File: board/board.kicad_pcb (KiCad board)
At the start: 2 copper layers, 0 parts

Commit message: board: try different footprint placements
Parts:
- added REF**: USB_C_Receptacle_HRO_TYPE-C-31-M-17, Connector_USB:USB_C_Receptacle_HRO_TYPE-C-31-M-17, F.Cu at (163.4, 135.4)
- added REF**: USB_C_Receptacle_GCT_USB4105-xx-A_16P_TopMnt_Horizontal, Connector_USB:USB_C_Receptacle_GCT_USB4105-xx-A_16P_TopMnt_Horizontal, F.Cu at (70.9, 41.3)
- added REF**: PinHeader_2x15_P1.00mm_Vertical, Connector_PinHeader_1.00mm:PinHeader_2x15_P1.00mm_Vertical, F.Cu at (99.8, 123.7)
- added REF**: ProMicro_Reversible_Single, PCM_marbastlib-xp-promicroish:ProMicro_Reversible_Single, F.Cu at (84.0, 140.1)
- added REF**: Hirose_FH12-20S-0.5SH_1x20-1MP_P0.50mm_Horizontal, Connector_FFC-FPC:Hirose_FH12-20S-0.5SH_1x20-1MP_P0.50mm_Horizontal, F.Cu at (103.5, 107.0)
- added REF**: USB_C_Receptacle_HRO_TYPE-C-31-M-17, Connector_USB:USB_C_Receptacle_HRO_TYPE-C-31-M-17, F.Cu at (163.4, 123.6)
- added REF**: USB_C_Receptacle_GCT_USB4105-xx-A_16P_TopMnt_Horizontal, Connector_USB:USB_C_Receptacle_GCT_USB4105-xx-A_16P_TopMnt_Horizontal, F.Cu at (123.3, 101.9)
- added REF**: DF40C-40DS-0.4V, phiboard:DF40C-40DS-0.4V, F.Cu at (52.1, 35.6)
- added REF**: Raytac_MDBT50Q, RF_Module:Raytac_MDBT50Q, F.Cu at (59.8, 36.8)
- added REF**: PinHeader_2x11_P2.54mm_Vertical, Connector_PinHeader_2.54mm:PinHeader_2x11_P2.54mm_Vertical, F.Cu at (113.5, 149.1)
- added REF**: USB_C_Receptacle_GCT_USB4105-xx-A_16P_TopMnt_Horizontal, Connector_USB:USB_C_Receptacle_GCT_USB4105-xx-A_16P_TopMnt_Horizontal, F.Cu at (178.2, 121.3)
- added REF**: JST_EH_S2B-EH_1x02_P2.50mm_Horizontal, Connector_JST:JST_EH_S2B-EH_1x02_P2.50mm_Horizontal, F.Cu at (185.1, 137.2)
- added REF**: USB_C_Receptacle_GCT_USB4105-xx-A_16P_TopMnt_Horizontal, Connector_USB:USB_C_Receptacle_GCT_USB4105-xx-A_16P_TopMnt_Horizontal, F.Cu at (70.9, 28.7)
- added REF**: Molex_54548-1071_1x10-1MP_P0.5mm_Horizontal, Connector_FFC-FPC:Molex_54548-1071_1x10-1MP_P0.5mm_Horizontal, F.Cu at (130.7, 107.0)
- added REF**: Raytac_MDBT50Q, RF_Module:Raytac_MDBT50Q, F.Cu at (112.2, 107.5)
- added REF**: USB_C_Receptacle_GCT_USB4105-xx-A_16P_TopMnt_Horizontal, Connector_USB:USB_C_Receptacle_GCT_USB4105-xx-A_16P_TopMnt_Horizontal, F.Cu at (123.3, 112.1)
- added REF**: Molex_54548-1071_1x10-1MP_P0.5mm_Horizontal, Connector_FFC-FPC:Molex_54548-1071_1x10-1MP_P0.5mm_Horizontal, F.Cu at (82.4, 34.9)
- added REF**: PinHeader_2x10_P1.00mm_Vertical, Connector_PinHeader_1.00mm:PinHeader_2x10_P1.00mm_Vertical, F.Cu at (105.2, 128.0)
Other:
- board outline added: 85 x 90.8 mm

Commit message: board: outline key matrix in pcb
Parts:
- removed the REF** at (70.9, 41.3)
- added REF**: JST_EH_S2B-EH_1x02_P2.50mm_Horizontal, Connector_JST:JST_EH_S2B-EH_1x02_P2.50mm_Horizontal, F.Cu at (86.5, 48.8)
- moved REF** 70.4 mm to (133.8, 170.6)
- moved REF** 70.4 mm to (153.6, 165.5)
- moved REF** 70.4 mm to (160.9, 170.6)
- moved REF** 70.4 mm to (142.5, 171.1)
- moved REF** 70.4 mm to (153.6, 175.7)
- moved REF** 12.1 mm to (42.3, 28.5), turned to 180 degrees
- moved REF** 4.04 mm to (74.9, 28.2)
- moved REF** 3.40 mm to (63.2, 36.6)
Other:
- board size 85 x 90.8 mm -> 132.3 x 154.3 mm

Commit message: board: change outline to flat 19 mm spacing (instead of 19.05 mm)
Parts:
- added REF**: JST_EH_S2B-EH_1x02_P2.50mm_Horizontal, Connector_JST:JST_EH_S2B-EH_1x02_P2.50mm_Horizontal, F.Cu at (85.0, 53.8)
- moved REF** 186.6 mm to (228.8, 26.6)
- moved REF** 186.6 mm to (249.8, 34.8)
- moved REF** 186.6 mm to (268.9, 33.0)
- moved REF** 186.6 mm to (273.1, 46.9)
- moved REF** 186.6 mm to (261.5, 26.3)
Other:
- board size 132.3 x 154.3 mm -> 146.8 x 156.2 mm

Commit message: board: start rough footprint placement
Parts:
- removed the REF** at (113.5, 149.1)
- added REF**: Raytac_MDBT50Q, RF_Module:Raytac_MDBT50Q, B.Cu at (99.3, 58.2)
- added REF**: USB_C_Receptacle_GCT_USB4105-xx-A_16P_TopMnt_Horizontal, Connector_USB:USB_C_Receptacle_GCT_USB4105-xx-A_16P_TopMnt_Horizontal, B.Cu at (110.7, 50.6)
- added REF**: XUNPU FPC-05FB-30PH20 1x30, phiboard:XUNPU FPC-05FB-30PH20 1x30, B.Cu at (119.0, 70.4)
- added REF**: Molex_54548-1071_1x10-1MP_P0.5mm_Horizontal, Connector_FFC-FPC:Molex_54548-1071_1x10-1MP_P0.5mm_Horizontal, B.Cu at (118.9, 57.0)
- REF**: moved to B.Cu
- moved REF** 3.38 mm to (87.0, 51.0), turned to -90 degrees

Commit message: board: pcb rough footprint placement
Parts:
- removed the REF** at (163.4, 135.4)
- removed the REF** at (163.4, 123.6)
- removed the REF** at (178.2, 121.3)
- removed the REF** at (185.1, 137.2)
- added C1: 10nF, Capacitor_SMD:C_0201_0603Metric, F.Cu at (246.2, 106.5)
- added C10: 10uF, Capacitor_SMD:C_0201_0603Metric, F.Cu at (208.6, 71.0)
- added C12: 1uF, Capacitor_SMD:C_0201_0603Metric, F.Cu at (214.6, 64.5)
- added C13: 2.2uF, Capacitor_SMD:C_0201_0603Metric, F.Cu at (211.8, 65.0)
- added C14: 1uF, Capacitor_SMD:C_0201_0603Metric, F.Cu at (211.8, 63.5)
- added C15: 10uF, Capacitor_SMD:C_0201_0603Metric, F.Cu at (201.2, 64.5)
- added C16: 10uF, Capacitor_SMD:C_0201_0603Metric, F.Cu at (201.2, 65.7)
- added C17: 10uF, Capacitor_SMD:C_0201_0603Metric, F.Cu at (204.8, 71.0)
- added C2: 10nF, Capacitor_SMD:C_0201_0603Metric, F.Cu at (193.7, 41.5)
- added C6: 1uF, Capacitor_SMD:C_0201_0603Metric, F.Cu at (205.5, 69.0)
- added C7: 12.5pF, Capacitor_SMD:C_0201_0603Metric, F.Cu at (175.6, 65.2)
- added C8: 12.5pF, Capacitor_SMD:C_0201_0603Metric, F.Cu at (172.8, 64.9)
- added C9: 10uF, Capacitor_SMD:C_0201_0603Metric, F.Cu at (211.8, 62.2)
- added D1: SMAJ6.5CA, phiboard:SMBJ6.5CA, F.Cu at (213.2, 48.2)
- added D10: SMAJ6.5CA, phiboard:SMBJ6.5CA, F.Cu at (212.9, 38.7)
- added D11: SMAJ6.5CA, phiboard:SMBJ6.5CA, F.Cu at (213.1, 43.2)
- added D2: SMAJ6.5CA, phiboard:SMBJ6.5CA, F.Cu at (244.4, 100.0)
- added D6: LED, LED_SMD:LED_0805_2012Metric, F.Cu at (208.9, 58.8)
- added D7: LED, LED_SMD:LED_0805_2012Metric, F.Cu at (206.7, 58.8)
- added D8: LED, LED_SMD:LED_0805_2012Metric, F.Cu at (204.5, 58.8)
- added J1: USB_C_Receptacle_USB2.0_16P, Connector_USB:USB_C_Receptacle_GCT_USB4105-xx-A_16P_TopMnt_Horizontal, F.Cu at (252.3, 103.7)
- added J2: Conn_01x10, phiboard:THD_0510-10CL-GF, F.Cu at (225.2, 64.0)
- added J3: Conn_01x06, phiboard:swd_pad, F.Cu at (179.7, 43.5)
- added J4: Conn_01x02, Connector_PinHeader_2.54mm:PinHeader_1x02_P2.54mm_Vertical, F.Cu at (207.6, 82.5)
- added J6: Conn_01x02, phiboard:magnetic connector 01x02P, F.Cu at (238.9, 103.9)
- added J7: Conn_01x30, phiboard:THD_0510-30CL-GF, F.Cu at (160.2, 54.2)
- added J8: USB_C_Receptacle_USB2.0_16P, Connector_USB:USB_C_Receptacle_GCT_USB4105-xx-A_16P_TopMnt_Horizontal, F.Cu at (201.8, 41.1)
- added J9: Conn_01x02, phiboard:magnetic connector 01x02P, F.Cu at (222.9, 45.0)
- added L1: 2.2uH, phiboard:L_0806_2016Metric, F.Cu at (198.3, 64.2)
- added R1: 300kR, Resistor_SMD:R_0201_0603Metric, F.Cu at (246.2, 107.5)
- added R10: 0R, Resistor_SMD:R_0201_0603Metric, F.Cu at (211.9, 66.3)
- added R11: 250-500kR, Resistor_SMD:R_0201_0603Metric, F.Cu at (207.5, 69.0)
- added R12: 10kR, Resistor_SMD:R_0201_0603Metric, F.Cu at (206.5, 69.0)
- added R13: 10kR, Resistor_SMD:R_0201_0603Metric, F.Cu at (206.8, 71.0)
- added R2: 5.1kR, Resistor_SMD:R_0201_0603Metric, F.Cu at (246.2, 104.9)
- added R3: 5.1kR, Resistor_SMD:R_0201_0603Metric, F.Cu at (246.2, 103.0)
- added R4: 300kR, Resistor_SMD:R_0201_0603Metric, F.Cu at (208.9, 45.0)
- added R5: 300kR, Resistor_SMD:R_0201_0603Metric, F.Cu at (193.9, 43.3)
- added R6: 10R, Resistor_SMD:R_0201_0603Metric, F.Cu at (203.5, 48.9)
- added R7: 10R, Resistor_SMD:R_0201_0603Metric, F.Cu at (203.6, 47.6)
- added R8: 10R, Resistor_SMD:R_0201_0603Metric, F.Cu at (199.6, 48.8)
- added R9: 10R, Resistor_SMD:R_0201_0603Metric, F.Cu at (199.7, 47.7)
- added U1: USBLC6-2SC6, Package_TO_SOT_SMD:SOT-23-6, F.Cu at (195.4, 48.1)
- added U2: nPM1300-QEAA, phiboard:nordic_npm1300-QEAA_qfn, F.Cu at (205.8, 64.3)
- added U3: MDBT50Q-P1MV2, RF_Module:Raytac_MDBT50Q, F.Cu at (184.3, 59.3)
- added Y1: 32k Hz, Crystal:Crystal_SMD_3215-2Pin_3.2x1.5mm, F.Cu at (175.6, 68.4)

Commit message: board: pcb re-link footprints
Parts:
- removed R4: 300kR, Resistor_SMD:R_0201_0603Metric
- removed REF** (x4): USB_C_Receptacle_GCT_USB4105-xx-A_16P_TopMnt_Horizontal, Connector_USB:USB_C_Receptacle_GCT_USB4105-xx-A_16P_TopMnt_Horizontal
- removed REF**: DF40C-40DS-0.4V, phiboard:DF40C-40DS-0.4V
- removed REF** (x3): Raytac_MDBT50Q, RF_Module:Raytac_MDBT50Q
- removed REF** (x2): JST_EH_S2B-EH_1x02_P2.50mm_Horizontal, Connector_JST:JST_EH_S2B-EH_1x02_P2.50mm_Horizontal
- removed REF**: XUNPU FPC-05FB-30PH20 1x30, phiboard:XUNPU FPC-05FB-30PH20 1x30
- removed REF** (x3): Molex_54548-1071_1x10-1MP_P0.5mm_Horizontal, Connector_FFC-FPC:Molex_54548-1071_1x10-1MP_P0.5mm_Horizontal
- removed REF**: PinHeader_2x10_P1.00mm_Vertical, Connector_PinHeader_1.00mm:PinHeader_2x10_P1.00mm_Vertical
- removed REF**: PinHeader_2x15_P1.00mm_Vertical, Connector_PinHeader_1.00mm:PinHeader_2x15_P1.00mm_Vertical
- removed REF**: ProMicro_Reversible_Single, PCM_marbastlib-xp-promicroish:ProMicro_Reversible_Single
- removed REF**: Hirose_FH12-20S-0.5SH_1x20-1MP_P0.50mm_Horizontal, Connector_FFC-FPC:Hirose_FH12-20S-0.5SH_1x20-1MP_P0.50mm_Horizontal
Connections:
- J2 pad MP: (no net) -> unconnected-(J2-MountPin-PadMP)_1
- J7 pad MP: (no net) -> unconnected-(J7-MountPin-PadMP)_1

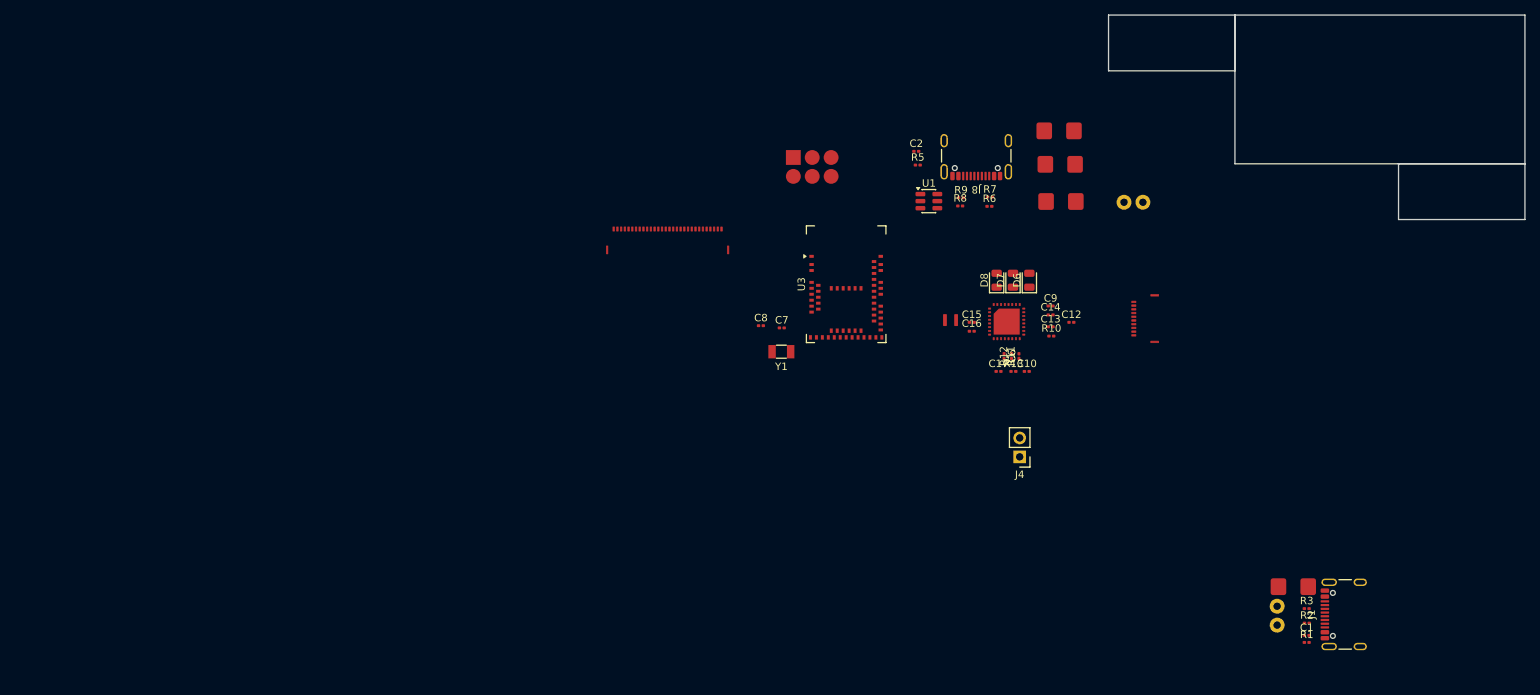
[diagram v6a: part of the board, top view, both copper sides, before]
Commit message: board: pcb move components to approximate location
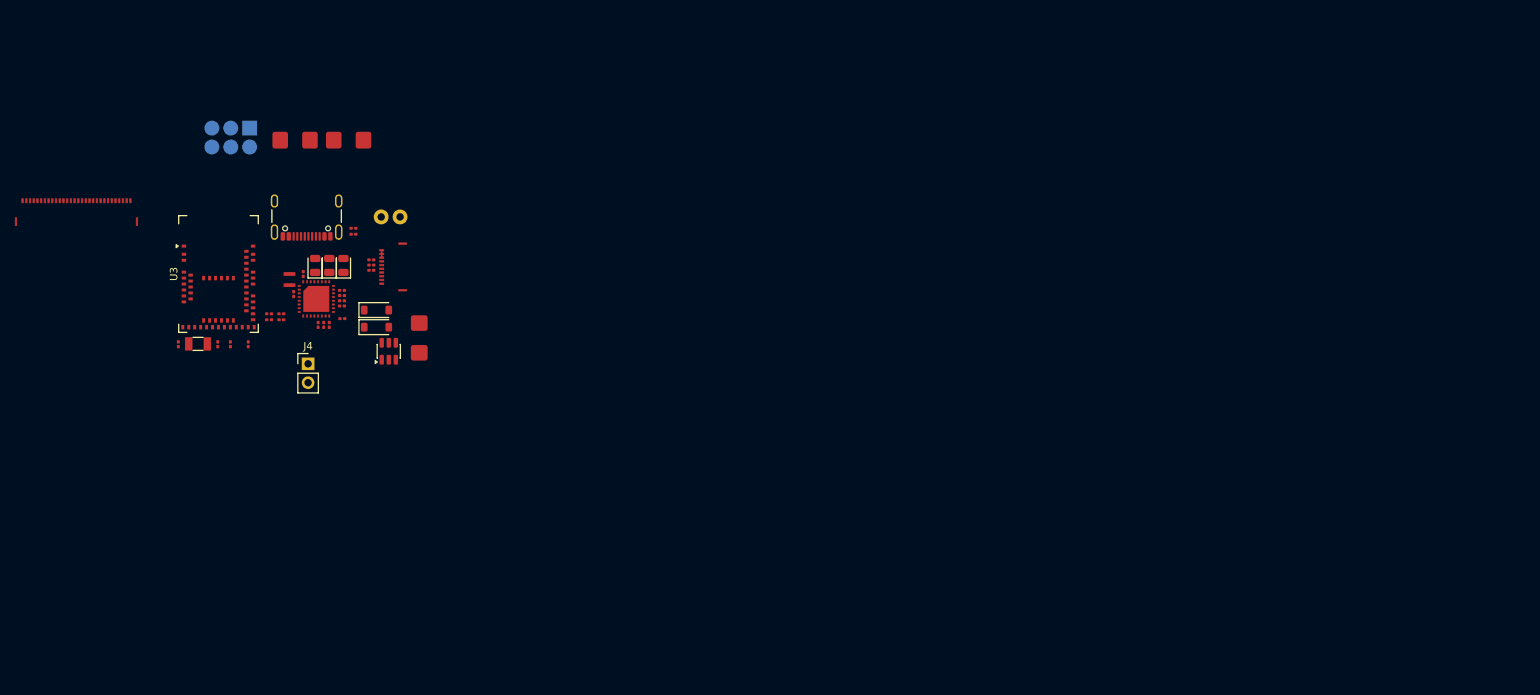
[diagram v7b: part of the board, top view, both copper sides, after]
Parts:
- removed C1: 10nF, Capacitor_SMD:C_0201_0603Metric
- removed D2: SMAJ6.5CA, phiboard:SMBJ6.5CA
- removed J1: USB_C_Receptacle_USB2.0_16P, Connector_USB:USB_C_Receptacle_GCT_USB4105-xx-A_16P_TopMnt_Horizontal
- removed J6: Conn_01x02, phiboard:magnetic connector 01x02P
- removed R1: 300kR, Resistor_SMD:R_0201_0603Metric
- removed R2, R3: 5.1kR, Resistor_SMD:R_0201_0603Metric
- added C3: 1uF, Capacitor_SMD:C_0201_0603Metric, F.Cu at (120.4, 56.8)
- added C4: 1uF, Capacitor_SMD:C_0201_0603Metric, F.Cu at (120.4, 56.0)
- added D3: D_Schottky, Diode_SMD:D_SOD-123, F.Cu at (121.1, 65.1)
- added D4: D_Schottky, Diode_SMD:D_SOD-123, F.Cu at (121.1, 62.8)
- C6: value 1uF -> 470pF
- J3: moved to B.Cu
- moved C9 108.0 mm to (103.8, 67.4), turned to -90 degrees
- moved C10 107.2 mm to (101.5, 67.4), turned to 90 degrees
- moved D11 103.0 mm to (110.2, 40.0), turned to 180 degrees
- moved J2 101.4 mm to (124.1, 57.0)
- moved J9 99.9 mm to (123.0, 47.0)
- moved C12 98.2 mm to (116.5, 60.9), turned to 180 degrees
- moved R6 98.1 mm to (106.7, 64.1)
- moved R7 96.7 mm to (108.3, 64.1)
- moved J4 96.5 mm to (111.9, 70.0), turned to 0 degrees
- moved D10 95.6 mm to (117.3, 40.0)
- moved R10 95.4 mm to (116.5, 64.0), turned to 180 degrees
- moved C14 95.4 mm to (116.5, 60.1)
- moved C13 95.3 mm to (116.5, 62.2)
- moved C17 94.4 mm to (111.2, 58.0), turned to 90 degrees
- moved R8 94.1 mm to (106.7, 63.3)
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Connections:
- J7 pad 27: key24 -> unconnected-(J7-Pin_27-Pad27)
- J7 pad 28: key25 -> +1V8
- J7 pad 29: key26 -> +3V3
- J7 pad 30: key27 -> GND
- U2 pad 15: unconnected-(U2-SHPHLD-Pad15) -> shphld
- U3 pad 10: unconnected-(U3-P0.29-Pad10) -> key13
- U3 pad 11: sclk -> key14
- U3 pad 12: unconnected-(U3-P0.31-Pad12) -> key15
- U3 pad 13: unconnected-(U3-P0.28-Pad13) -> key16
- U3 pad 14: unconnected-(U3-P0.30-Pad14) -> key17
- U3 pad 16: unconnected-(U3-P0.27-Pad16) -> key1
- U3 pad 19: unconnected-(U3-P0.26-Pad19) -> key2
- U3 pad 20: scs -> key3
- U3 pad 21: unconnected-(U3-P0.05-Pad21) -> key4
- U3 pad 22: unconnected-(U3-P0.06-Pad22) -> key5
- U3 pad 23: unconnected-(U3-P0.07-Pad23) -> key6
- U3 pad 24: unconnected-(U3-P0.08-Pad24) -> key7
- U3 pad 27: unconnected-(U3-P0.11-Pad27) -> key8
- U3 pad 29: unconnected-(U3-P0.12-Pad29) -> key9
- U3 pad 36: unconnected-(U3-P0.14-Pad36) -> key10
- U3 pad 37: unconnected-(U3-P0.13-Pad37) -> scl
- U3 pad 38: unconnected-(U3-P0.16-Pad38) -> key11
- U3 pad 39: unconnected-(U3-P0.15-Pad39) -> sda
- U3 pad 41: unconnected-(U3-P0.17-Pad41) -> shphld
- U3 pad 42: unconnected-(U3-P0.19-Pad42) -> key18
- U3 pad 43: unconnected-(U3-P0.21-Pad43) -> key19
- U3 pad 44: unconnected-(U3-P0.20-Pad44) -> sclk
- U3 pad 45: unconnected-(U3-P0.23-Pad45) -> key20
- U3 pad 46: unconnected-(U3-P0.22-Pad46) -> si
- U3 pad 48: unconnected-(U3-P0.24-Pad48) -> scs
- U3 pad 49: unconnected-(U3-P0.25-Pad49) -> key21
- U3 pad 52: unconnected-(U3-P0.09-Pad52) -> key22
- U3 pad 54: unconnected-(U3-P0.10-Pad54) -> key23
- U3 pad 9: si -> key12
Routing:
- net GND: track 0.00 -> 1.00 mm
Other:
- board size 146.8 x 156.2 mm -> 36.5 x 17.5 mm

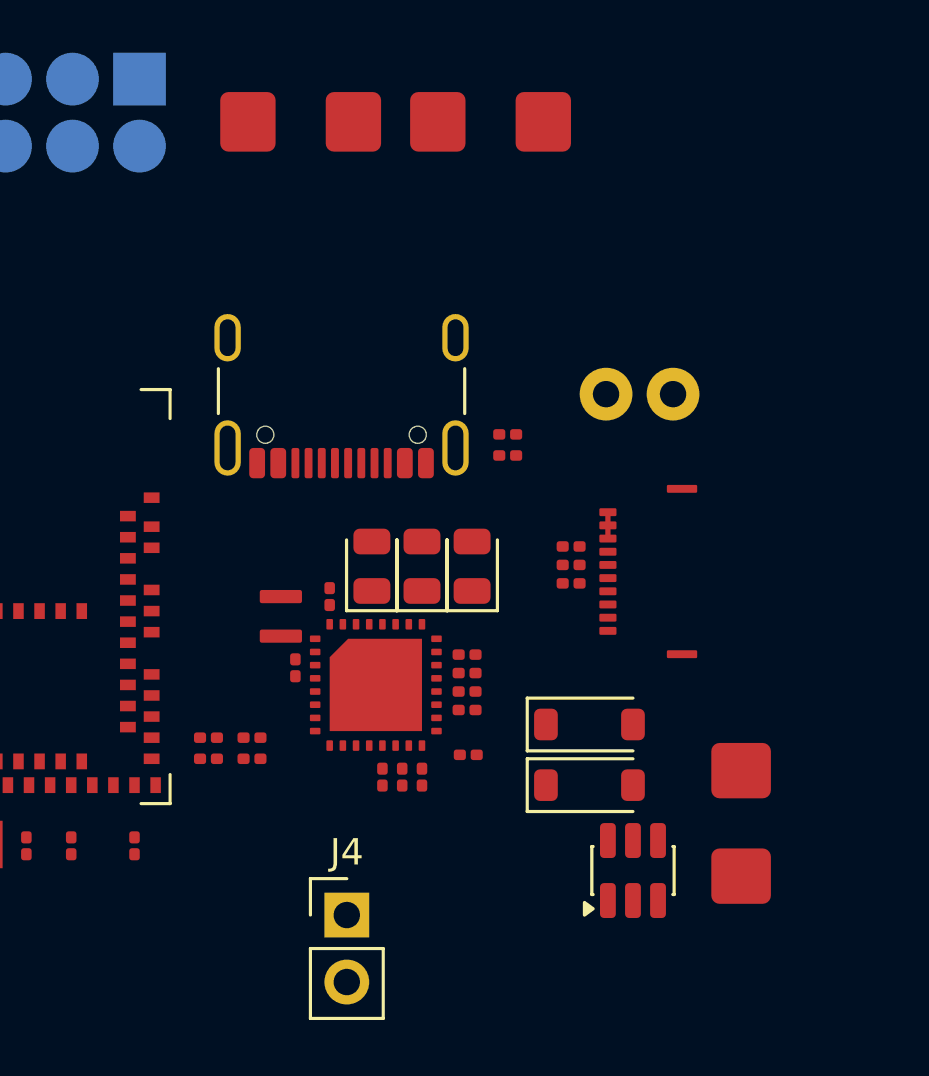
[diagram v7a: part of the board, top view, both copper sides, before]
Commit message: board: pcb implement schematic changes in pcb
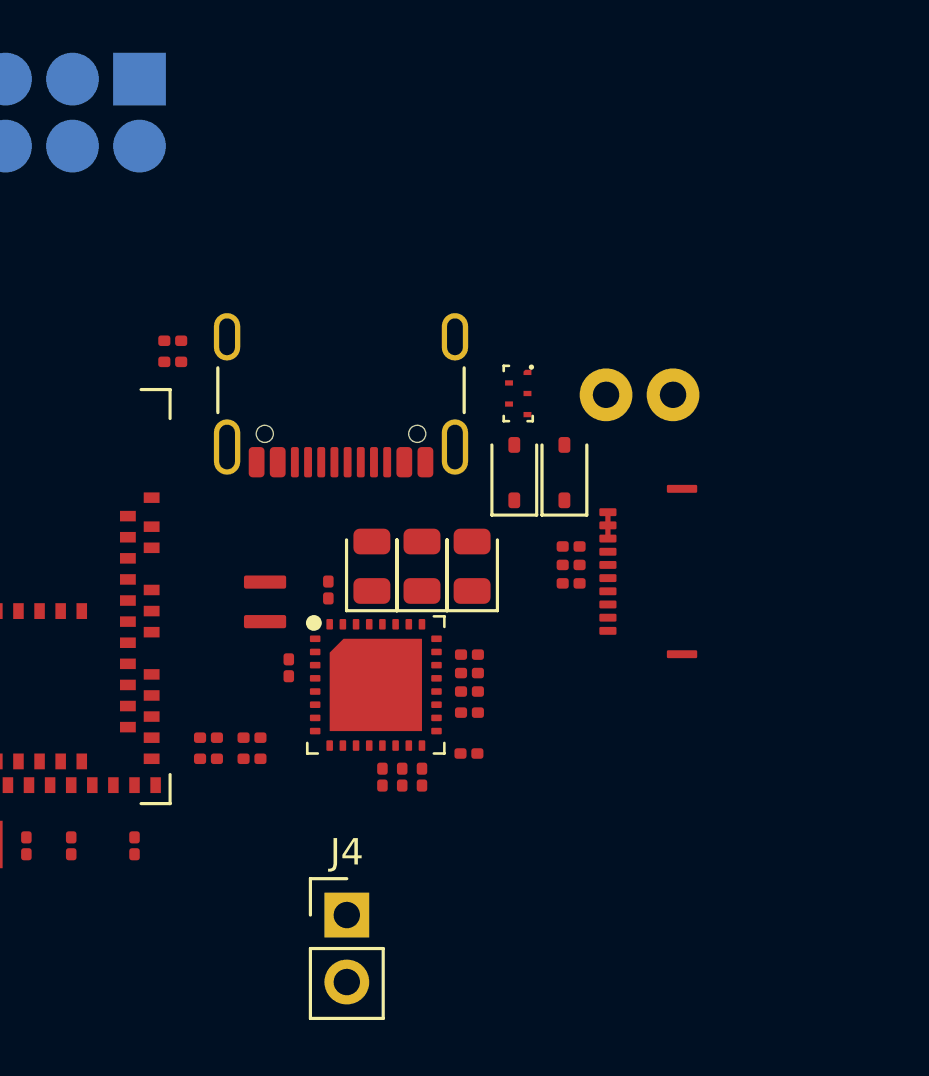
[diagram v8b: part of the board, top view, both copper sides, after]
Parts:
- removed D1, D10, D11: SMAJ6.5CA, phiboard:SMBJ6.5CA
- removed U1: USBLC6-2SC6, Package_TO_SOT_SMD:SOT-23-6
- added U4: TVS_Array, phiboard:DFN2010, F.Cu at (118.4, 50.2)
- D3, D4: footprint Diode_SMD:D_SOD-123 -> Diode_SMD:D_SOD-323
- moved C2 13.2 mm to (105.3, 49.0)
- moved R5 13.2 mm to (105.3, 48.2)
- moved D3 12.2 mm to (118.2, 53.2), turned to 90 degrees
- moved D4 9.60 mm to (120.2, 53.2), turned to 90 degrees
- moved L1 0.81 mm to (108.8, 58.1)
- moved C17 0.25 mm to (111.2, 57.7)
- moved C16 0.25 mm to (109.7, 60.6)
- moved C13 0.13 mm to (116.5, 62.4)
- moved C12 0.09 mm to (116.5, 60.9)
- moved C14 0.09 mm to (116.5, 60.1)
- moved C15 0.09 mm to (116.5, 61.5)
- moved R10 0.06 mm to (116.5, 63.9)
- turned R6 to 180 degrees
- turned R7 to 180 degrees
- turned R8 to 180 degrees
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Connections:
- D3 pad 1: vusb_raw -> vbus_raw
- D4 pad 1: vusb_raw -> vbus_raw
- J8 pad A5: cc1 -> Net-(J8-CC1)
- J8 pad B5: cc2 -> Net-(J8-CC2)
- U2 pad 23: cc1 -> unconnected-(U2-CC1-Pad23)
- U2 pad 24: cc2 -> unconnected-(U2-CC2-Pad24)
